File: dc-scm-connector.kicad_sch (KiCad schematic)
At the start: 55 parts, among them J1 PCB-Edge_DC-SCM-2.1_2x84_Rev-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

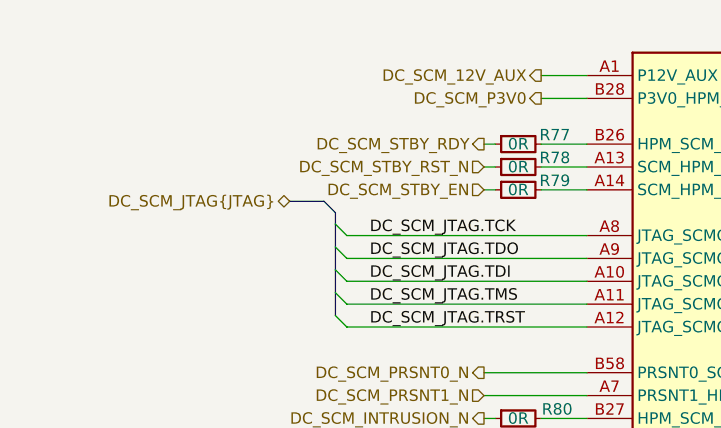
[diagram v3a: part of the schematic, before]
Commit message: [#83148] Add level shifters for i2c & stby
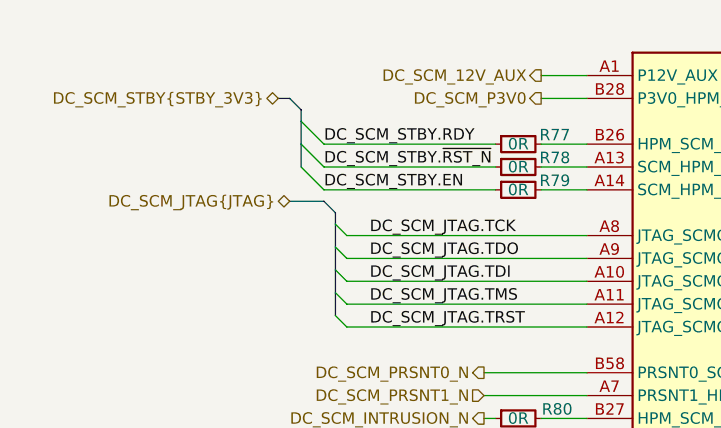
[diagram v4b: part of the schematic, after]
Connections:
- net DC_SCM_STBY_EN renamed DC_SCM_STBY.EN
- net DC_SCM_STBY_RDY renamed DC_SCM_STBY.RDY
- net DC_SCM_STBY_RST_N renamed DC_SCM_STBY.~{RST_N}
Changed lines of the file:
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@@
 	)
 	(bus_entry
+		(at 41.91 54.61)
+		(size 2.54 2.54)
+		(stroke
+			(width 0)
+			(type default)
+		)
+	)
+	(bus_entry
 		(at 41.91 176.53)
 		(size 1.27 1.27)
@@
 	)
 	(bus_entry
+		(at 41.91 52.07)
+		(size 2.54 2.54)
+		(stroke
+			(width 0)
+			(type default)
+		)
+	)
+	(bus_entry
 		(at 173.99 124.46)
 		(size -1.27 1.27)
@@
 	)
 	(bus_entry
+		(at 41.91 49.53)
+		(size 2.54 2.54)
+		(stroke
+			(width 0)
+			(type default)
+		)
+	)
+	(bus_entry
 		(at 345.44 149.86)
 		(size -1.27 1.27)
@@
 		)
 	)
+	(bus
+		(pts
+			(xy 41.91 49.53) (xy 41.91 52.07)
+		)
+		(stroke
+			(width 0)
+			(type default)
+		)
+	)
 	(wire
 		(pts
@@
 	(wire
 		(pts
+			(xy 44.45 57.15) (xy 63.5 57.15)
+		)
+		(stroke
+			(width 0)
+			(type default)
+		)
+	)
+	(wire
+		(pts
 			(xy 68.58 82.55) (xy 73.66 82.55)
 		)
@@
 		)
 	)
+	(bus
+		(pts
+			(xy 179.07 113.03) (xy 175.26 113.03)
+		)
+		(stroke
+			(width 0)
+			(type default)
+		)
+	)
 	(wire
 		(pts
-			(xy 62.23 54.61) (xy 63.5 54.61)
+			(xy 165.1 67.31) (xy 146.05 67.31)
 		)
 		(stroke
@@
 	(bus
 		(pts
-			(xy 179.07 113.03) (xy 175.26 113.03)
+			(xy 175.26 125.73) (xy 173.99 127)
 		)
 		(stroke
@@
 	(wire
 		(pts
-			(xy 165.1 67.31) (xy 146.05 67.31)
+			(xy 73.66 142.24) (xy 68.58 142.24)
 		)
 		(stroke
@@
 	(bus
 		(pts
-			(xy 175.26 125.73) (xy 173.99 127)
+			(xy 41.91 48.26) (xy 41.91 49.53)
 		)
 		(stroke
@@
 	(wire
 		(pts
-			(xy 73.66 142.24) (xy 68.58 142.24)
+			(xy 135.89 110.49) (xy 140.97 110.49)
 		)
 		(stroke
@@
 	(wire
 		(pts
-			(xy 135.89 110.49) (xy 140.97 110.49)
+			(xy 311.15 109.22) (xy 344.17 109.22)
 		)
 		(stroke
@@
 		)
 	)
-	(wire
+	(bus
 		(pts
-			(xy 311.15 109.22) (xy 344.17 109.22)
+			(xy 41.91 52.07) (xy 41.91 54.61)
 		)
 		(stroke
@@
 	(wire
 		(pts
-			(xy 62.23 52.07) (xy 63.5 52.07)
-		)
-		(stroke
-			(width 0)
-			(type default)
-		)
-	)
-	(wire
-		(pts
 			(xy 68.58 170.18) (xy 73.66 170.18)
 		)
@@
 	(wire
 		(pts
+			(xy 44.45 54.61) (xy 63.5 54.61)
+		)
+		(stroke
+			(width 0)
+			(type default)
+		)
+	)
+	(wire
+		(pts
 			(xy 135.89 151.13) (xy 140.97 151.13)
 		)
@@
 	(wire
 		(pts
-			(xy 62.23 57.15) (xy 63.5 57.15)
-		)
-		(stroke
-			(width 0)
-			(type default)
-		)
-	)
-	(wire
-		(pts
 			(xy 135.89 135.89) (xy 140.97 135.89)
 		)
@@
 		)
 	)
+	(bus
+		(pts
+			(xy 39.37 46.99) (xy 40.64 46.99)
+		)
+		(stroke
+			(width 0)
+			(type default)
+		)
+	)
 	(wire
 		(pts
@@
 	(wire
 		(pts
+			(xy 44.45 52.07) (xy 63.5 52.07)
+		)
+		(stroke
+			(width 0)
+			(type default)
+		)
+	)
+	(wire
+		(pts
 			(xy 135.89 201.93) (xy 160.02 201.93)
 		)
@@
 		)
 	)
+	(bus
+		(pts
+			(xy 41.91 48.26) (xy 40.64 46.99)
+		)
+		(stroke
+			(width 0)
+			(type default)
+		)
+	)
 	(wire
 		(pts
@@
 		)
 	)
+	(label "DC_SCM_STBY.~{RST_N}"
+		(at 44.45 54.61 0)
+		(effects
+			(font
+				(size 1.27 1.27)
+			)
+			(justify left bottom)
+		)
+	)
 	(label "DC_SCM_I2C_I3C17.SCL"
 		(at 146.05 142.24 0)
@@
 		)
 	)
+	(label "DC_SCM_STBY.RDY"
+		(at 44.45 52.07 0)
+		(effects
+			(font
+				(size 1.27 1.27)
+			)
+			(justify left bottom)
+		)
+	)
 	(label "DC-SCM_CLK_100M_1.CLK+"
 		(at 314.96 91.44 0)
@@
 		)
 	)
+	(label "DC_SCM_STBY.EN"
+		(at 44.45 57.15 0)
+		(effects
+			(font
+				(size 1.27 1.27)
+			)
+			(justify left bottom)
+		)
+	)
 	(label "DC_SCM_TPM_SPI.SCK"
 		(at 44.45 175.26 0)
@@
 		)
 	)
-	(hierarchical_label "DC_SCM_STBY_EN"
-		(shape input)
-		(at 62.23 57.15 180)
-		(effects
-			(font
-				(size 1.27 1.27)
-			)
-			(justify right)
-		)
-	)
 	(hierarchical_label "DC_SCM_PECI"
 		(shape bidirectional)
@@
 		)
 	)
+	(hierarchical_label "DC_SCM_STBY{STBY_3V3}"
+		(shape bidirectional)
+		(at 39.37 46.99 180)
+		(effects
+			(font
+				(size 1.27 1.27)
+			)
+			(justify right)
+		)
+	)
 	(hierarchical_label "DC_SCM_I2C_I3C15{I2C}"
 		(shape bidirectional)
@@
 		)
 	)
-	(hierarchical_label "DC_SCM_STBY_RDY"
-		(shape output)
-		(at 62.23 52.07 180)
-		(effects
-			(font
-				(size 1.27 1.27)
-			)
-			(justify right)
-		)
-	)
-	(hierarchical_label "DC_SCM_STBY_RST_N"
-		(shape input)
-		(at 62.23 54.61 180)
-		(effects
-			(font
-				(size 1.27 1.27)
-			)
-			(justify right)
-		)
-	)

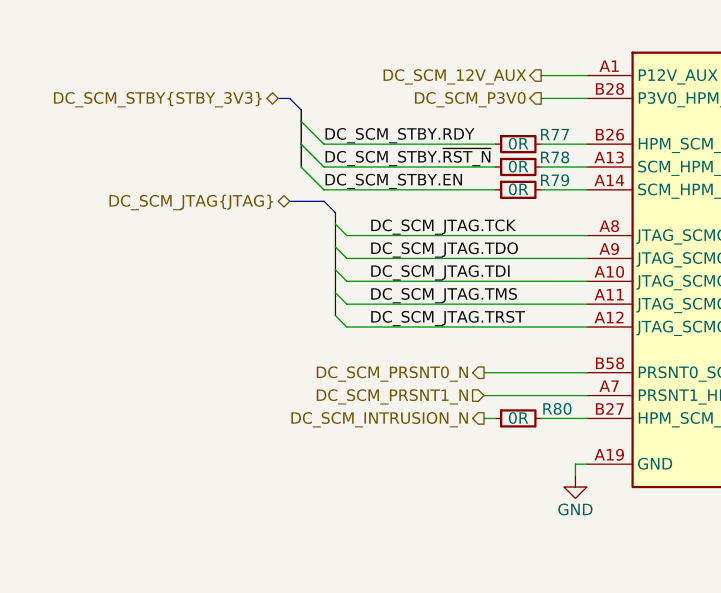
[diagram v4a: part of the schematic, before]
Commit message: [#83148] Connect the level shifters, change STBY bus to individual signals
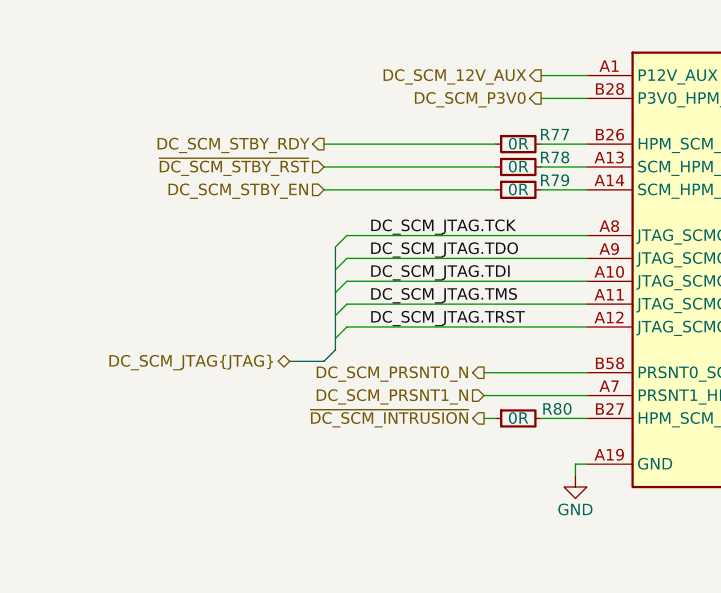
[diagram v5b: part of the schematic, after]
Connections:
- net DC_SCM_INTRUSION_N renamed ~{DC_SCM_INTRUSION}
- net DC_SCM_STBY.EN renamed DC_SCM_STBY_EN
- net DC_SCM_STBY.RDY renamed DC_SCM_STBY_RDY
- net DC_SCM_STBY.~{RST_N} renamed ~{DC_SCM_STBY_RST}

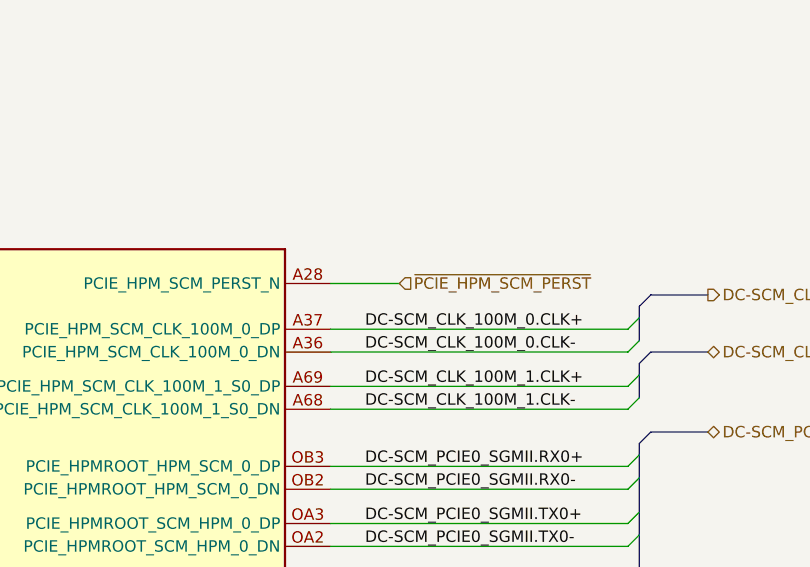
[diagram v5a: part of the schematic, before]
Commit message: [#83338] Low speed PCIe x4 connections
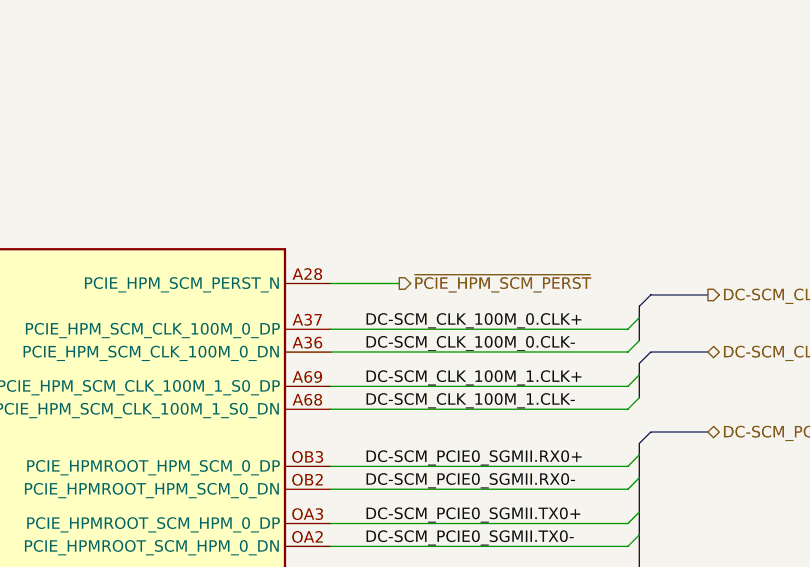
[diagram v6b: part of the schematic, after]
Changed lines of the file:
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@@
 	)
 	(hierarchical_label "~{PCIE_HPM_SCM_PERST}"
-		(shape input)
+		(shape output)
 		(at 318.77 80.01 0)
 		(effects

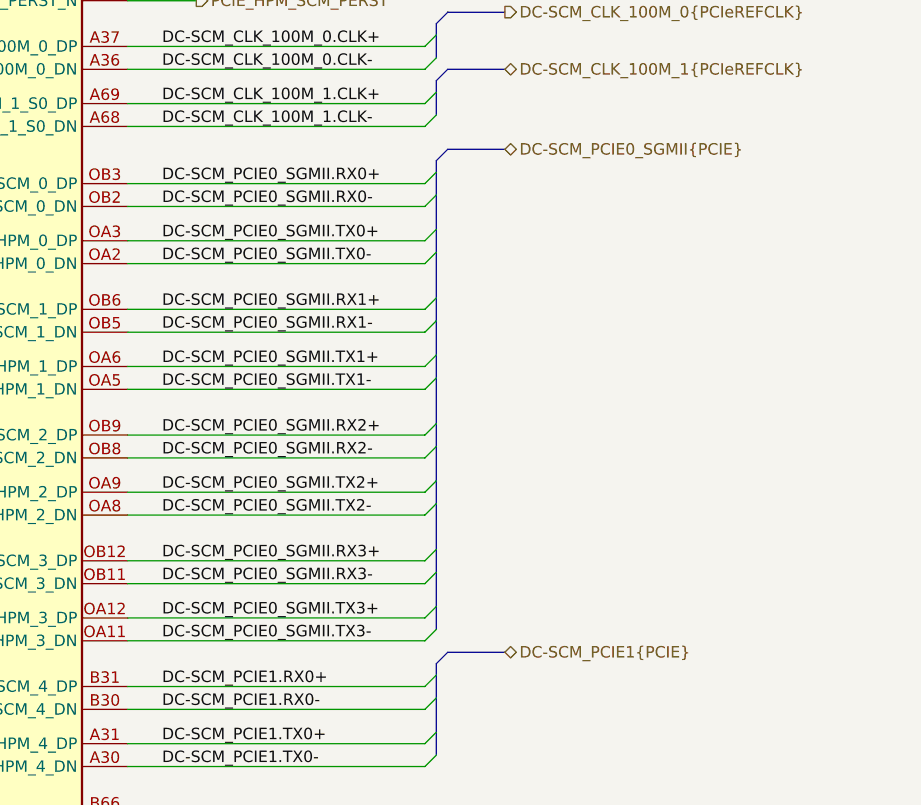
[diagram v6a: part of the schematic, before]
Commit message: [#83338] Fixed PCIe TX/RX
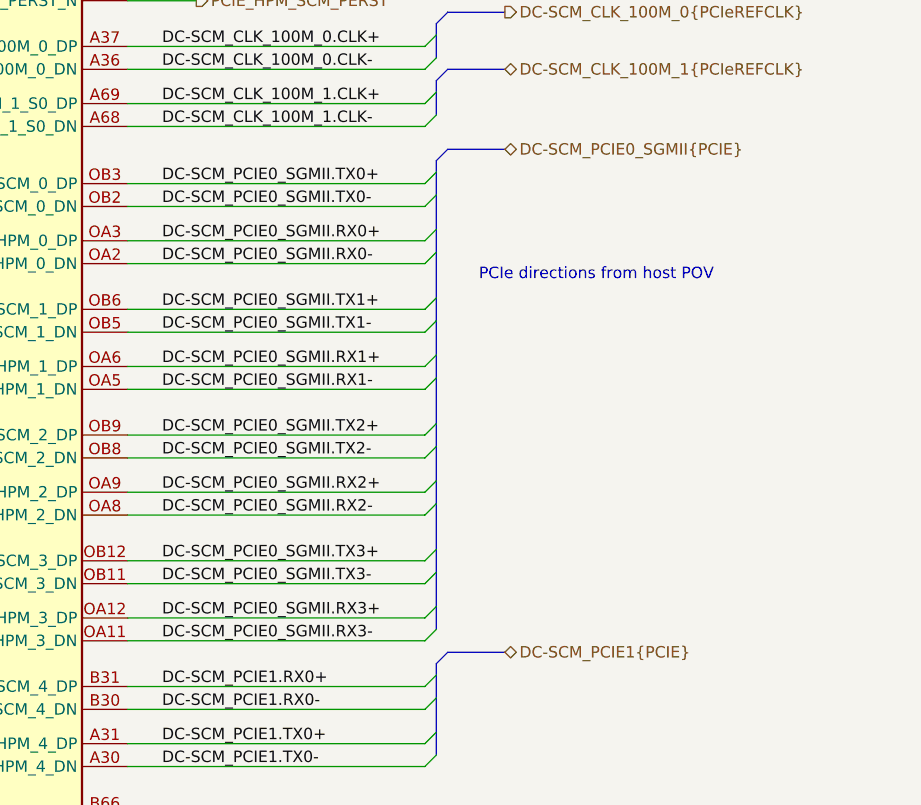
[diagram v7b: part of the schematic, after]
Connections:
- net DC-SCM_PCIE0_SGMII.RX0+: now also J1.OA3 (PCIE_HPMROOT_SCM_HPM_0_DP); no longer J1.OB3 (PCIE_HPMROOT_HPM_SCM_0_DP)
- net DC-SCM_PCIE0_SGMII.RX0-: now also J1.OA2 (PCIE_HPMROOT_SCM_HPM_0_DN); no longer J1.OB2 (PCIE_HPMROOT_HPM_SCM_0_DN)
- net DC-SCM_PCIE0_SGMII.RX1+: now also J1.OA6 (PCIE_HPMROOT_SCM_HPM_1_DP); no longer J1.OB6 (PCIE_HPMROOT_HPM_SCM_1_DP)
- net DC-SCM_PCIE0_SGMII.RX1-: now also J1.OA5 (PCIE_HPMROOT_SCM_HPM_1_DN); no longer J1.OB5 (PCIE_HPMROOT_HPM_SCM_1_DN)
- net DC-SCM_PCIE0_SGMII.RX2+: now also J1.OA9 (PCIE_HPMROOT_SCM_HPM_2_DP); no longer J1.OB9 (PCIE_HPMROOT_HPM_SCM_2_DP)
- net DC-SCM_PCIE0_SGMII.RX2-: now also J1.OA8 (PCIE_HPMROOT_SCM_HPM_2_DN); no longer J1.OB8 (PCIE_HPMROOT_HPM_SCM_2_DN)
- net DC-SCM_PCIE0_SGMII.RX3+: now also J1.OA12 (PCIE_HPMROOT_SCM_HPM_3_DP); no longer J1.OB12 (PCIE_HPMROOT_HPM_SCM_3_DP)
- net DC-SCM_PCIE0_SGMII.RX3-: now also J1.OA11 (PCIE_HPMROOT_SCM_HPM_3_DN); no longer J1.OB11 (PCIE_HPMROOT_HPM_SCM_3_DN)
- net DC-SCM_PCIE0_SGMII.TX0+: now also J1.OB3 (PCIE_HPMROOT_HPM_SCM_0_DP); no longer J1.OA3 (PCIE_HPMROOT_SCM_HPM_0_DP)
- net DC-SCM_PCIE0_SGMII.TX0-: now also J1.OB2 (PCIE_HPMROOT_HPM_SCM_0_DN); no longer J1.OA2 (PCIE_HPMROOT_SCM_HPM_0_DN)
- net DC-SCM_PCIE0_SGMII.TX1+: now also J1.OB6 (PCIE_HPMROOT_HPM_SCM_1_DP); no longer J1.OA6 (PCIE_HPMROOT_SCM_HPM_1_DP)
- net DC-SCM_PCIE0_SGMII.TX1-: now also J1.OB5 (PCIE_HPMROOT_HPM_SCM_1_DN); no longer J1.OA5 (PCIE_HPMROOT_SCM_HPM_1_DN)
- net DC-SCM_PCIE0_SGMII.TX2+: now also J1.OB9 (PCIE_HPMROOT_HPM_SCM_2_DP); no longer J1.OA9 (PCIE_HPMROOT_SCM_HPM_2_DP)
- net DC-SCM_PCIE0_SGMII.TX2-: now also J1.OB8 (PCIE_HPMROOT_HPM_SCM_2_DN); no longer J1.OA8 (PCIE_HPMROOT_SCM_HPM_2_DN)
- net DC-SCM_PCIE0_SGMII.TX3+: now also J1.OB12 (PCIE_HPMROOT_HPM_SCM_3_DP); no longer J1.OA12 (PCIE_HPMROOT_SCM_HPM_3_DP)
- net DC-SCM_PCIE0_SGMII.TX3-: now also J1.OB11 (PCIE_HPMROOT_HPM_SCM_3_DN); no longer J1.OA11 (PCIE_HPMROOT_SCM_HPM_3_DN)
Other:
- note added: "PCIe directions from host POV"
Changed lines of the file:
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@@
 		(rev "1.0.0")
 	)
+	(text "PCIe directions from host POV"
+		(exclude_from_sim no)
+		(at 363.22 110.49 0)
+		(effects
+			(font
+				(size 1.27 1.27)
+			)
+		)
+	)
 	(text "TODO: add PECI voltage translator"
 		(exclude_from_sim no)
@@
 	)
 	(label "DC-SCM_PCIE0_SGMII.RX1-"
-		(at 314.96 116.84 0)
+		(at 314.96 123.19 0)
 		(effects
 			(font
@@
 	)
 	(label "DC-SCM_PCIE0_SGMII.TX1+"
-		(at 314.96 120.65 0)
+		(at 314.96 114.3 0)
 		(effects
 			(font
@@
 	)
 	(label "DC-SCM_PCIE0_SGMII.RX0+"
-		(at 314.96 100.33 0)
+		(at 314.96 106.68 0)
 		(effects
 			(font
@@
 	)
 	(label "DC-SCM_PCIE0_SGMII.TX3+"
-		(at 314.96 148.59 0)
+		(at 314.96 142.24 0)
 		(effects
 			(font
@@
 	)
 	(label "DC-SCM_PCIE0_SGMII.RX2+"
-		(at 314.96 128.27 0)
+		(at 314.96 134.62 0)
 		(effects
 			(font
@@
 	)
 	(label "DC-SCM_PCIE0_SGMII.TX0+"
-		(at 314.96 106.68 0)
+		(at 314.96 100.33 0)
 		(effects
 			(font
@@
 	)
 	(label "DC-SCM_PCIE0_SGMII.RX0-"
-		(at 314.96 102.87 0)
+		(at 314.96 109.22 0)
 		(effects
 			(font
@@
 	)
 	(label "DC-SCM_PCIE0_SGMII.TX0-"
-		(at 314.96 109.22 0)
+		(at 314.96 102.87 0)
 		(effects
 			(font
@@
 	)
 	(label "DC-SCM_PCIE0_SGMII.TX1-"
-		(at 314.96 123.19 0)
+		(at 314.96 116.84 0)
 		(effects
 			(font
@@
 	)
 	(label "DC-SCM_PCIE0_SGMII.RX3+"
-		(at 314.96 142.24 0)
+		(at 314.96 148.59 0)
 		(effects
 			(font
@@
 	)
 	(label "DC-SCM_PCIE0_SGMII.RX3-"
-		(at 314.96 144.78 0)
+		(at 314.96 151.13 0)
 		(effects
 			(font
@@
 	)
 	(label "DC-SCM_PCIE0_SGMII.RX1+"
-		(at 314.96 114.3 0)
+		(at 314.96 120.65 0)
 		(effects
 			(font
@@
 	)
 	(label "DC-SCM_PCIE0_SGMII.RX2-"
-		(at 314.96 130.81 0)
+		(at 314.96 137.16 0)
 		(effects
 			(font
@@
 	)
 	(label "DC-SCM_PCIE0_SGMII.TX2+"
-		(at 314.96 134.62 0)
+		(at 314.96 128.27 0)
 		(effects
 			(font
@@
 	)
 	(label "DC-SCM_PCIE0_SGMII.TX3-"
-		(at 314.96 151.13 0)
+		(at 314.96 144.78 0)
 		(effects
 			(font
@@
 	)
 	(label "DC-SCM_PCIE0_SGMII.TX2-"
-		(at 314.96 137.16 0)
+		(at 314.96 130.81 0)
 		(effects
 			(font

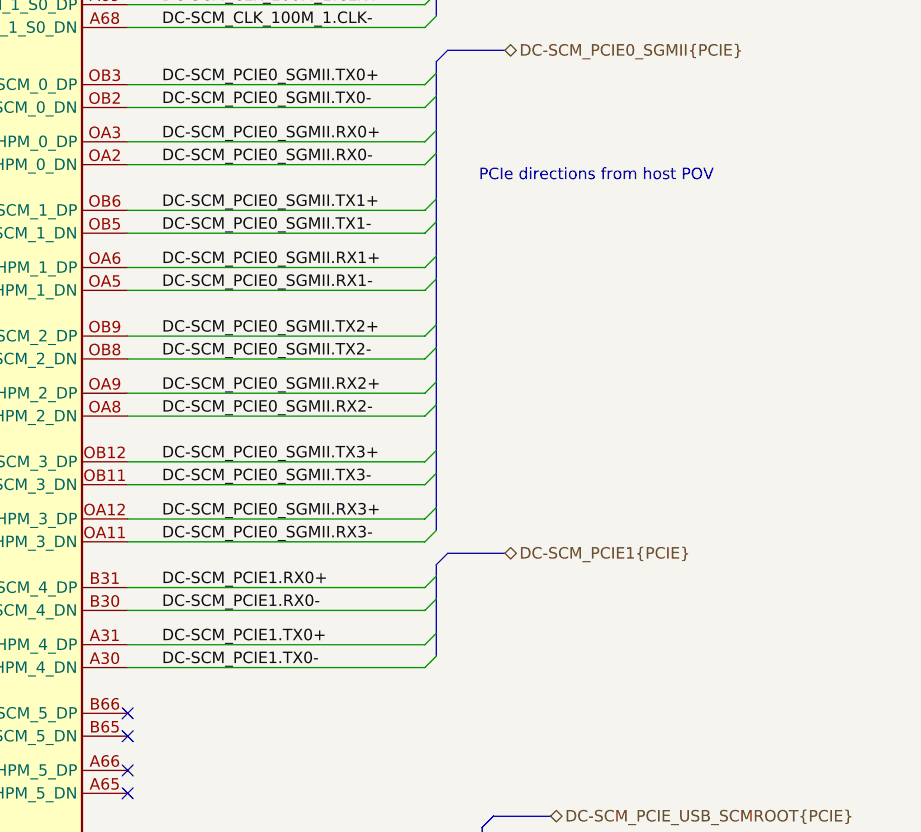
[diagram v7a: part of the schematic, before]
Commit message: [#83338] Fixed HS connection AC caps and TX/RX swaps
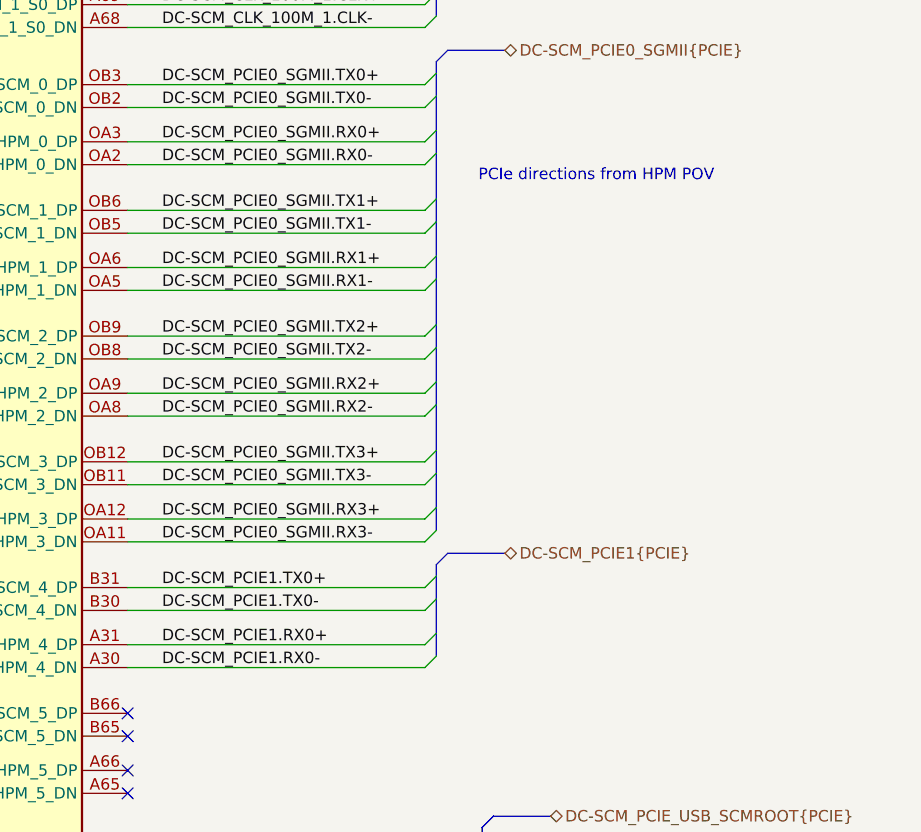
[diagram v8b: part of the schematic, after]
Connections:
- net DC-SCM_PCIE1.RX0+: now also J1.A31 (PCIE_HPMROOT_SCM_HPM_4_DP); no longer J1.B31 (PCIE_HPMROOT_HPM_SCM_4_DP)
- net DC-SCM_PCIE1.RX0-: now also J1.A30 (PCIE_HPMROOT_SCM_HPM_4_DN); no longer J1.B30 (PCIE_HPMROOT_HPM_SCM_4_DN)
- net DC-SCM_PCIE1.TX0+: now also J1.B31 (PCIE_HPMROOT_HPM_SCM_4_DP); no longer J1.A31 (PCIE_HPMROOT_SCM_HPM_4_DP)
- net DC-SCM_PCIE1.TX0-: now also J1.B30 (PCIE_HPMROOT_HPM_SCM_4_DN); no longer J1.A30 (PCIE_HPMROOT_SCM_HPM_4_DN)
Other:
- note added: "PCIe directions from HPM POV"
- note removed: "PCIe directions from host POV"
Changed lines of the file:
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@@
 		(rev "1.0.0")
 	)
-	(text "PCIe directions from host POV"
+	(text "PCIe directions from HPM POV\n"
 		(exclude_from_sim no)
 		(at 363.22 110.49 0)
@@
 	)
 	(label "DC-SCM_PCIE1.RX0-"
-		(at 314.96 158.75 0)
+		(at 314.96 165.1 0)
 		(effects
 			(font
@@
 	)
 	(label "DC-SCM_PCIE1.RX0+"
-		(at 314.96 156.21 0)
+		(at 314.96 162.56 0)
 		(effects
 			(font
@@
 	)
 	(label "DC-SCM_PCIE1.TX0+"
-		(at 314.96 162.56 0)
+		(at 314.96 156.21 0)
 		(effects
 			(font
@@
 	)
 	(label "DC-SCM_PCIE1.TX0-"
-		(at 314.96 165.1 0)
+		(at 314.96 158.75 0)
 		(effects
 			(font
